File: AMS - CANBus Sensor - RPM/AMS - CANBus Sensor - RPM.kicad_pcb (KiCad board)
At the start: 4 copper layers, 50.4 x 49.6 mm, 30 parts, among them J1 ICSP, J2 TTL_Programmer, J4 Conn_01x02, J5 Power_And_CAN, J6 Conn_02x08_Odd_Even, Q1 IRF9Z34NPBF, U1 ATmega328P-P, U2 178.6165.0001, U3 MCP2551-I-SN, U4 MCP2515-xSO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

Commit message: wip for RPM
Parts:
- added C10: 0.1uF, Capacitor_THT:C_Disc_D7.5mm_W5.0mm_P10.00mm, F.Cu at (63.2, 67.2)
- added C11: 68uF, Capacitor_THT:CP_Radial_D8.0mm_P5.00mm, F.Cu at (54.2, 71.7)
- added C12: 0.02uF, Capacitor_SMD:C_0805_2012Metric_Pad1.18x1.45mm_HandSolder, F.Cu at (74.2, 87.4)
- added C13: 1uF, Capacitor_THT:CP_Radial_D4.0mm_P1.50mm, F.Cu at (85.0, 73.3)
- added C8: 0.1uF, Capacitor_THT:C_Disc_D7.5mm_W5.0mm_P10.00mm, F.Cu at (63.2, 60.7)
- added C9: 120uF, Capacitor_THT:CP_Radial_D8.0mm_P5.00mm, F.Cu at (54.2, 62.2)
- added D2: 1N5817, SamacSys_Parts:DIOAD1414W86L464D238, F.Cu at (73.4, 83.9)
- added IC1: MAX764CPA+, SamacSys_Parts:DIP762W56P254L938H457Q8N, F.Cu at (66.6, 76.2)
- added IC2: LM2917N-8_NOPB, SamacSys_Parts:DIP794W53P254L959H508Q8N, F.Cu at (80.5, 63.3)
- added IC4: OPA2340UA_2K5, SamacSys_Parts:SOIC127P600X175-8N, F.Cu at (61.9, 98.2)
- added J3: Conn_01x02, Connector_PinHeader_2.54mm:PinHeader_1x02_P2.54mm_Vertical, F.Cu at (63.8, 84.3)
- added J7: Conn_01x02, Connector_PinHeader_2.54mm:PinHeader_1x02_P2.54mm_Vertical, F.Cu at (68.4, 84.3)
- added J8: Conn_01x01, Connector_PinHeader_2.54mm:PinHeader_1x01_P2.54mm_Vertical, F.Cu at (60.0, 103.7)
- added L1: 47uH, Inductor_THT:L_Axial_L7.0mm_D3.3mm_P10.16mm_Horizontal_Fastron_MICC, F.Cu at (73.4, 79.4)
- added R10: 120k, Resistor_SMD:R_1206_3216Metric_Pad1.30x1.75mm_HandSolder, F.Cu at (54.7, 96.6)
- added R11: 100k, Resistor_SMD:R_1206_3216Metric_Pad1.30x1.75mm_HandSolder, F.Cu at (54.7, 84.7)
- added R12: 470, Resistor_SMD:R_1206_3216Metric_Pad1.30x1.75mm_HandSolder, F.Cu at (54.7, 88.0)
- added R13: 15k, Resistor_SMD:R_1206_3216Metric_Pad1.30x1.75mm_HandSolder, F.Cu at (54.7, 99.9)
- added R14: 47k, Resistor_SMD:R_1206_3216Metric_Pad1.30x1.75mm_HandSolder, F.Cu at (54.7, 103.2)
- added R15: 47k, Resistor_SMD:R_1206_3216Metric_Pad1.30x1.75mm_HandSolder, F.Cu at (54.7, 106.5)
- added R16: 100k, Resistor_SMD:R_1206_3216Metric_Pad1.30x1.75mm_HandSolder, F.Cu at (54.7, 91.3)
- added R8: 10k, Resistor_SMD:R_1206_3216Metric_Pad1.30x1.75mm_HandSolder, F.Cu at (54.7, 78.1)
- added R9: 22k, Resistor_SMD:R_1206_3216Metric_Pad1.30x1.75mm_HandSolder, F.Cu at (54.7, 81.4)
- added RV1: 100k, Potentiometer_THT:Potentiometer_Bourns_3296W_Vertical, F.Cu at (79.9, 73.7)
- J6: value Conn_02x08_Odd_Even -> Conn_01x02; footprint Connector_PinHeader_2.54mm:PinHeader_2x08_P2.54mm_Vertical -> Connector_PinHeader_2.54mm:PinHeader_1x02_P2.54mm_Vertical
- U2: value 178.6165.0001 -> 3568; footprint SamacSys_Parts:17861650001 -> SamacSys_Parts:3568
- moved Powerboard1 72.9 mm to (152.3, 136.2), turned to 90 degrees
- moved U1 63.6 mm to (140.3, 121.7), turned to 90 degrees
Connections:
- J6 pad 1: +5V -> Net-(J6-Pin_1)
- J6 pad 2: /BareMinAtmel328P/PD3-D3 -> Net-(IC2-TACH+)
- U2 pad 1: +VDC -> Net-(Q1-Pad3)
- U2 pad 2: +VDC -> Net-(Q1-Pad3)
- U2 pad 3: Net-(Q1-Pad3) -> +VDC
- U2 pad 4: Net-(Q1-Pad3) -> +VDC
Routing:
- net GND: track 192.8 -> 0.00 mm
- net +5V: track 112.4 -> 0.00 mm, vias 1 -> 0
- net /BareMinAtmel328P/RESET: track 75.7 -> 0.00 mm, vias 1 -> 0
- net +VDC: track 67.5 -> 0.00 mm
- net /BareMinAtmel328P/PB5-D13-SCK: track 42.0 -> 0.00 mm, vias 1 -> 0
- net /BareMinAtmel328P/PD0-RX: track 41.1 -> 0.00 mm
- net /BareMinAtmel328P/PB3-D11-MOSI: track 40.3 -> 0.00 mm
- net /BareMinAtmel328P/PC4-A4-SDA: track 40.0 -> 0.00 mm
- net /BareMinAtmel328P/PC0-A0: track 39.5 -> 0.00 mm
- net /BareMinAtmel328P/PB1-D9: track 38.5 -> 0.00 mm
- net /BareMinAtmel328P/PB4-D12-MISO: track 37.3 -> 0.00 mm
- net Net-(U4-OSC2): track 36.9 -> 0.00 mm, vias 1 -> 0
- net /BareMinAtmel328P/PD1-TX: track 36.3 -> 0.00 mm
- net /BareMinAtmel328P/PC5-A5-SCL: track 35.6 -> 0.00 mm
- net /BareMinAtmel328P/PC3-A3: track 35.5 -> 0.00 mm
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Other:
- board size 50.4 x 49.6 mm -> 56.9 x 41.9 mm

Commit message: fixing the same powerboard problem on the remaining boards.
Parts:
- moved Powerboard1 5.05 mm to (157.4, 136.2), turned to -90 degrees
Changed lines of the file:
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@@
 	(footprint "Connector_PinHeader_2.54mm:PinHeader_1x03_P2.54mm_Vertical"
 		(layer "F.Cu")
-		(at 152.300694 136.203605 90)
+		(at 157.350694 136.203605 -90)
 		(descr "Through hole straight pin header, 1x03, 2.54mm pitch, single row")
 		(tags "Through hole pin header THT 1x03 2.54mm single row")
 		(property "Reference" "Powerboard1"
-			(at -2.653373 2.208433 360)
+			(at 2.665399 2.314583 180)
 			(layer "F.SilkS")
 			(effects
@@
 		)
 		(property "Value" "Conn_01x03"
-			(at 0 7.41 270)
+			(at 0 7.41 90)
 			(layer "F.Fab")
 			(hide yes)
@@
 		)
 		(property "Footprint" "Connector_PinHeader_2.54mm:PinHeader_1x03_P2.54mm_Vertical"
-			(at 0 0 90)
+			(at 0 0 -90)
 			(unlocked yes)
 			(layer "F.Fab")
@@
 		)
 		(property "Datasheet" ""
-			(at 0 0 90)
+			(at 0 0 -90)
 			(unlocked yes)
 			(layer "F.Fab")
@@
 		)
 		(property "Description" ""
-			(at 0 0 90)
+			(at 0 0 -90)
 			(unlocked yes)
 			(layer "F.Fab")
@@
 		(attr through_hole)
 		(fp_line
-			(start -1.33 -1.33)
-			(end 0 -1.33)
+			(start -1.33 6.41)
+			(end 1.33 6.41)
 			(stroke
 				(width 0.12)
@@
 		)
 		(fp_line
-			(start -1.33 0)
-			(end -1.33 -1.33)
+			(start -1.33 1.27)
+			(end -1.33 6.41)
 			(stroke
 				(width 0.12)
@@
 		)
 		(fp_line
-			(start 1.33 1.27)
-			(end 1.33 6.41)
+			(start -1.33 1.27)
+			(end 1.33 1.27)
 			(stroke
 				(width 0.12)
@@
 		)
 		(fp_line
-			(start -1.33 1.27)
-			(end 1.33 1.27)
+			(start 1.33 1.27)
+			(end 1.33 6.41)
 			(stroke
 				(width 0.12)
@@
 		)
 		(fp_line
-			(start -1.33 1.27)
-			(end -1.33 6.41)
+			(start -1.33 0)
+			(end -1.33 -1.33)
 			(stroke
 				(width 0.12)
@@
 		)
 		(fp_line
-			(start -1.33 6.41)
-			(end 1.33 6.41)
+			(start -1.33 -1.33)
+			(end 0 -1.33)
 			(stroke
 				(width 0.12)
@@
 		)
 		(fp_line
-			(start 1.8 -1.8)
-			(end -1.8 -1.8)
+			(start -1.8 6.85)
+			(end 1.8 6.85)
 			(stroke
 				(width 0.05)
@@
 		)
 		(fp_line
-			(start -1.8 -1.8)
-			(end -1.8 6.85)
+			(start 1.8 6.85)
+			(end 1.8 -1.8)
 			(stroke
 				(width 0.05)
@@
 		)
 		(fp_line
-			(start 1.8 6.85)
-			(end 1.8 -1.8)
+			(start -1.8 -1.8)
+			(end -1.8 6.85)
 			(stroke
 				(width 0.05)
@@
 		)
 		(fp_line
-			(start -1.8 6.85)
-			(end 1.8 6.85)
+			(start 1.8 -1.8)
+			(end -1.8 -1.8)
 			(stroke
 				(width 0.05)
@@
 		)
 		(fp_line
-			(start 1.27 -1.27)
-			(end 1.27 6.35)
+			(start -1.27 6.35)
+			(end -1.27 -0.635)
 			(stroke
 				(width 0.1)
@@
 		)
 		(fp_line
-			(start -0.635 -1.27)
-			(end 1.27 -1.27)
+			(start 1.27 6.35)
+			(end -1.27 6.35)
 			(stroke
 				(width 0.1)
@@
 		)
 		(fp_line
-			(start 1.27 6.35)
-			(end -1.27 6.35)
+			(start -0.635 -1.27)
+			(end 1.27 -1.27)
 			(stroke
 				(width 0.1)
@@
 		)
 		(fp_line
-			(start -1.27 6.35)
-			(end -1.27 -0.635)
+			(start 1.27 -1.27)
+			(end 1.27 6.35)
 			(stroke
 				(width 0.1)
@@
 		)
 		(fp_text user "${REFERENCE}"
-			(at -2.635793 2.19541 360)
+			(at -2.635793 2.19541 180)
 			(layer "F.Fab")
 			(effects
@@
 		)
 		(pad "1" thru_hole rect
-			(at 0 0 90)
+			(at 0 0 270)
 			(size 1.7 1.7)
 			(drill 1)
@@
 		)
 		(pad "2" thru_hole oval
-			(at 0 2.54 90)
+			(at 0 2.54 270)
 			(size 1.7 1.7)
 			(drill 1)
@@
 		)
 		(pad "3" thru_hole oval
-			(at 0 5.08 90)
+			(at 0 5.08 270)
 			(size 1.7 1.7)
 			(drill 1)
@@
 		(tags "THT DIP DIL PDIP 2.54mm 7.62mm 300mil")
 		(property "Reference" "U1"
-			(at 3.894194 2.002959 270)
+			(at 3.894194 2.002959 -90)
 			(layer "F.SilkS")
 			(effects
@@
 		)
 		(property "Value" "ATmega328P-P"
-			(at 3.81 35.35 270)
+			(at 3.81 35.35 -90)
 			(layer "F.Fab")
 			(effects
@@
 		)
 		(fp_text user "${REFERENCE}"
-			(at 3.81 16.51 270)
+			(at 3.81 16.51 -90)
 			(layer "F.Fab")
 			(effects
@@
 		)
 	)
-	(group ""
-		(members "32d36bf8-48cf-4267-906c-74f1c392b87a" "46aaad29-9aaa-4ace-9280-7dd969f2eae3"
-			"8478962b-2080-4d70-b43a-9d4cb028e94d" "9efcbc6c-605d-444a-88a8-00e5131257d3"
-			"de113007-52bb-47cb-bf53-4f0f5eb4aa6b"
-		)
-	)

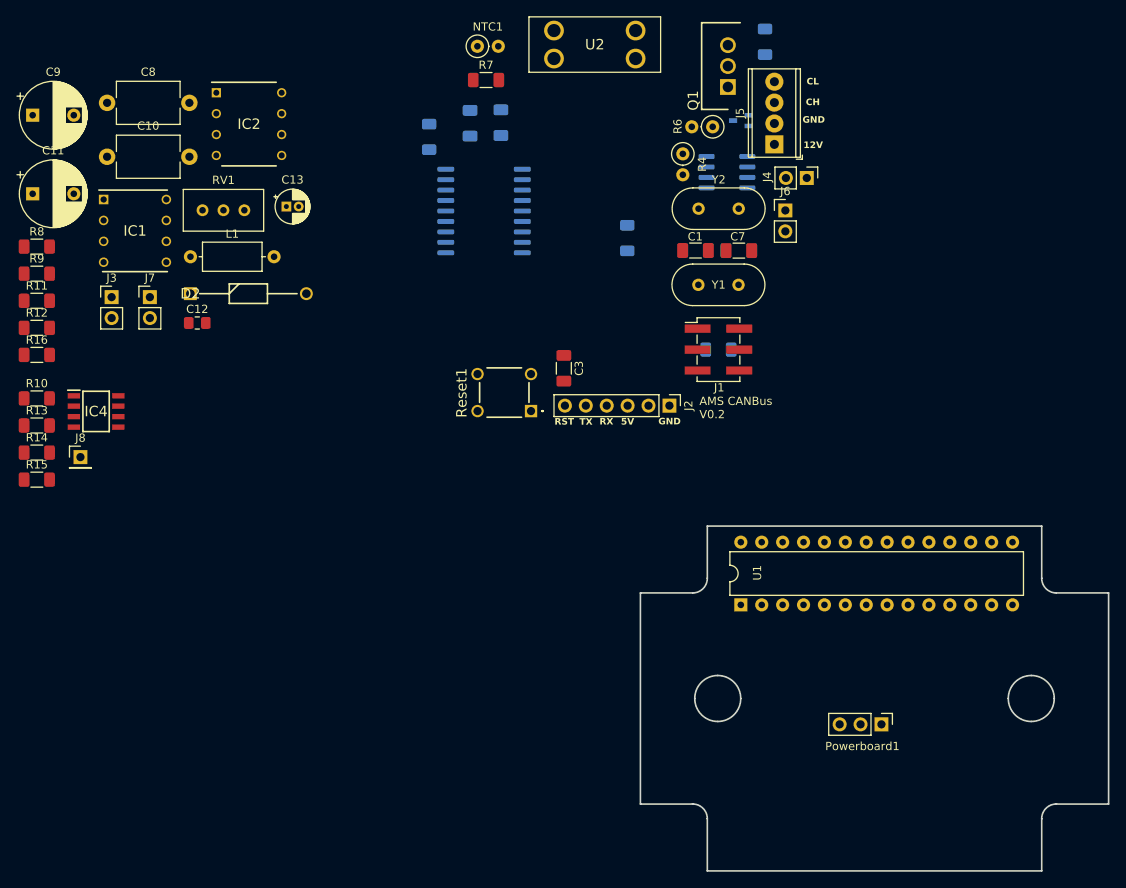
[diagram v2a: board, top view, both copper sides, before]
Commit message: RPM Sensor is done.
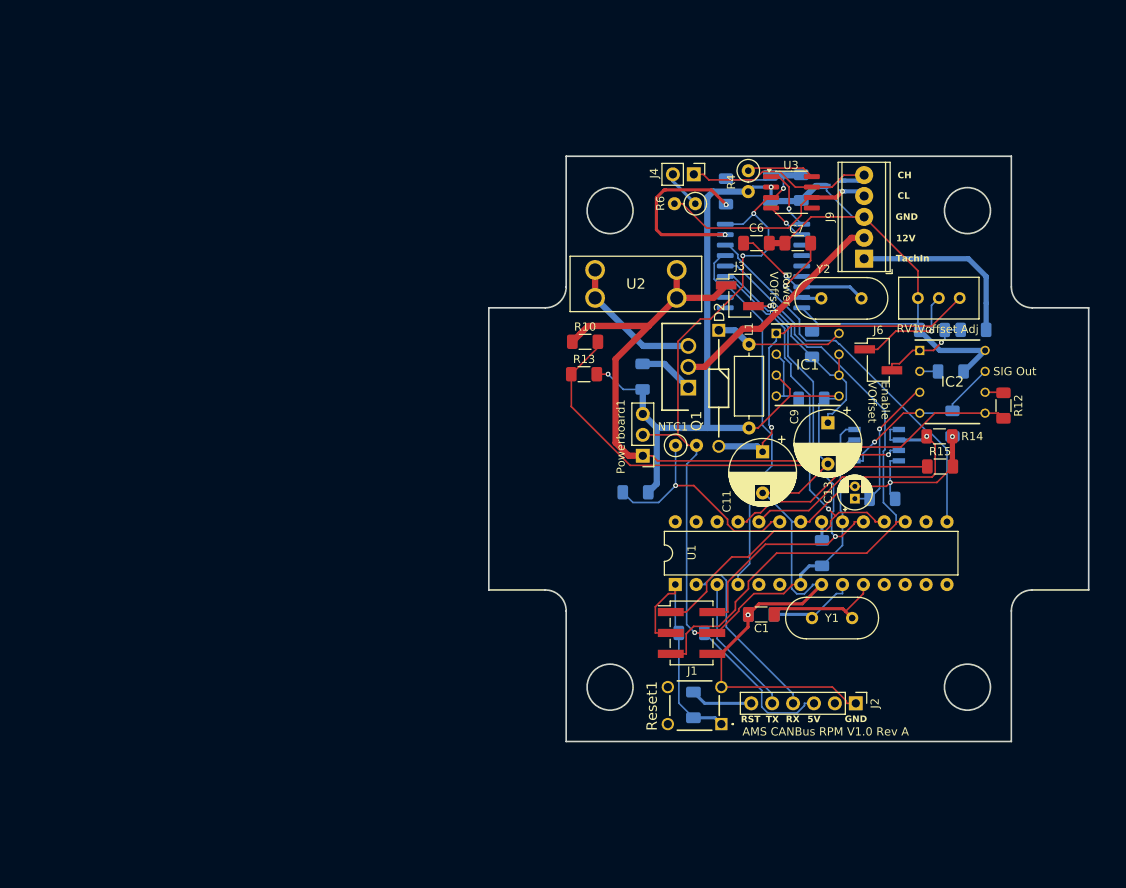
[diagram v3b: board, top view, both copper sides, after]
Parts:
- removed J5: Power_And_CAN, TerminalBlock_Phoenix:TerminalBlock_Phoenix_MPT-0,5-4-2.54_1x04_P2.54mm_Horizontal
- removed J7: Conn_01x02, Connector_PinHeader_2.54mm:PinHeader_1x02_P2.54mm_Vertical
- removed J8: Conn_01x01, Connector_PinHeader_2.54mm:PinHeader_1x01_P2.54mm_Vertical
- added J9: Screw_Terminal_01x05, TerminalBlock_Phoenix:TerminalBlock_Phoenix_MPT-0,5-5-2.54_1x05_P2.54mm_Horizontal, F.Cu at (155.2, 79.6)
- C10, C8: footprint Capacitor_THT:C_Disc_D7.5mm_W5.0mm_P10.00mm -> Resistor_SMD:R_1206_3216Metric_Pad1.30x1.75mm_HandSolder; moved to B.Cu
- C12: footprint Capacitor_SMD:C_0805_2012Metric_Pad1.18x1.45mm_HandSolder -> Resistor_SMD:R_1206_3216Metric_Pad1.30x1.75mm_HandSolder; moved to B.Cu
- C3, IC4, R11, R16, R7, R8, R9: moved to B.Cu
- C6, U3: moved to F.Cu
- J3, J6: footprint Connector_PinHeader_2.54mm:PinHeader_1x02_P2.54mm_Vertical -> Connector_PinHeader_2.54mm:PinHeader_1x02_P2.54mm_Vertical_SMD_Pin1Left
- moved R12 117.9 mm to (172.2, 97.5), turned to -90 degrees
- moved R8 114.3 mm to (168.5, 88.3), turned to 180 degrees
- moved R16 111.6 mm to (166.0, 99.7), turned to -90 degrees
- moved R15 109.8 mm to (164.5, 104.9)
- moved R14 109.7 mm to (164.4, 101.2)
- moved R9 109.0 mm to (163.5, 88.3), turned to 180 degrees
- moved R11 105.5 mm to (157.5, 108.8)
- moved C9 103.6 mm to (150.8, 99.6), turned to -90 degrees
- moved IC4 95.0 mm to (156.8, 102.3), turned to 180 degrees
- moved C11 94.1 mm to (142.9, 103.1), turned to -90 degrees
- moved C8 92.8 mm to (148.8, 96.6)
- moved C12 91.8 mm to (165.8, 93.3)
- moved IC2 91.0 mm to (166.0, 94.6)
- moved C10 88.6 mm to (148.9, 90.0), turned to 90 degrees
- moved RV1 87.6 mm to (166.9, 84.4)
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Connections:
- IC2 pad 4: Net-(IC2-EMIT) -> /RPM_Sensor/RPM-Vout
- IC2 pad 7: Net-(IC2-EMIT) -> /RPM_Sensor/RPM-Vout
- R16 pad 1: Net-(IC2-EMIT) -> /RPM_Sensor/RPM-Vout
- R8 pad 1: /RPM_Sensor/TachIn -> TachIn
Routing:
- net GND: track 0.00 -> 264.7 mm, vias 0 -> 5
- net +5V: track 0.00 -> 141.8 mm, vias 0 -> 4
- net +VDC: track 0.00 -> 92.9 mm
- net /BareMinAtmel328P/PB3-D11-MOSI: track 0.00 -> 80.6 mm
- net /BareMinAtmel328P/PB4-D12-MISO: track 0.00 -> 72.2 mm, vias 0 -> 1
- net /BareMinAtmel328P/PB5-D13-SCK: track 0.00 -> 63.4 mm, vias 0 -> 1
- net Net-(IC4-+IN_A): track 0.00 -> 52.2 mm, vias 0 -> 1
- net /BareMinAtmel328P/PB1-D9: track 0.00 -> 46.9 mm
- net Net-(IC1-OUT): track 0.00 -> 45.0 mm, vias 0 -> 1
- net /BareMinAtmel328P/PD2-D2: track 0.00 -> 40.0 mm
- net /BareMinAtmel328P/PC1-A1: track 0.00 -> 35.8 mm, vias 0 -> 1
- net /BareMinAtmel328P/PC2-A2: track 0.00 -> 30.4 mm, vias 0 -> 1
- net /BareMinAtmel328P/RESET: track 0.00 -> 28.9 mm
- net /BareMinAtmel328P/PC0-A0: track 0.00 -> 28.5 mm, vias 0 -> 1
- net Net-(J9-Pin_2): track 0.00 -> 27.9 mm
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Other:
- board size 56.9 x 41.9 mm -> 72.9 x 71.1 mm
- copper layers 4 -> 2
- board text added: "AMS CANBus RPM V1.0 Rev A"
- board text added: "Enable VOffset"
- board text added: "Power VOffset"
- board text added: "SIG Out"
- board text added: "TachIn"
- board text added: "Voffset Adj"
- board text removed: "AMS CANBus V0.2"
